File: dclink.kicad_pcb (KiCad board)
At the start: 2 copper layers, 61.5 x 59.5 mm, 3 parts, among them U1 mounting_holes, U2 dcb-310

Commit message: better shape
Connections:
- net Net-(U1-Pad) renamed GND
- U1 pad 2: Net-(U1-Pad)_1 -> VDC
- U2 pad 3: Net-(U1-Pad)_1 -> VDC
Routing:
- net VDC: vias 0 -> 60
- net Net-(U1-Pad)_1: vias 60 -> 0
- added copper zone on B.Cu, net VDC
- added copper zone on F.Cu, net VDC
- removed copper zone on B.Cu, net Net-(U1-Pad)_1
- removed copper zone on F.Cu, net Net-(U1-Pad)_1
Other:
- outline, holes or cut-outs redrawn

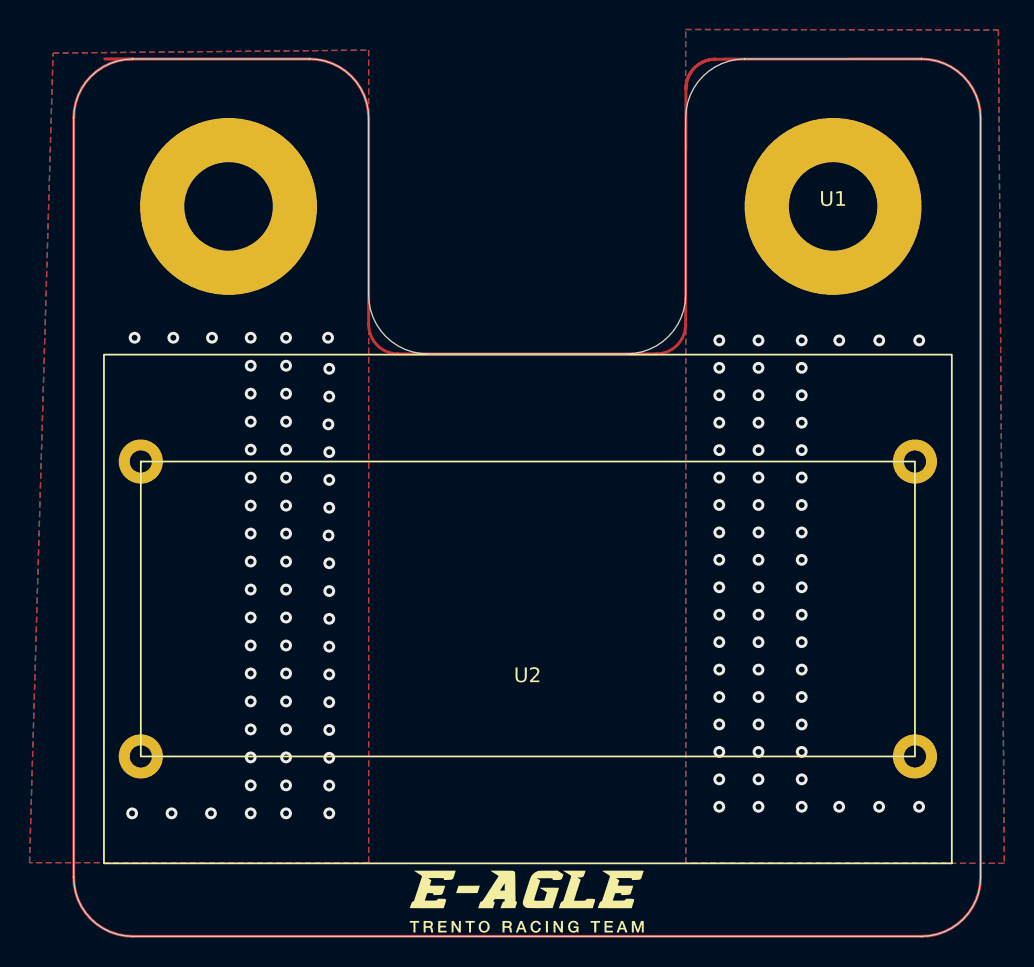
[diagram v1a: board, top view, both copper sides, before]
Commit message: first half vias, todo: top border
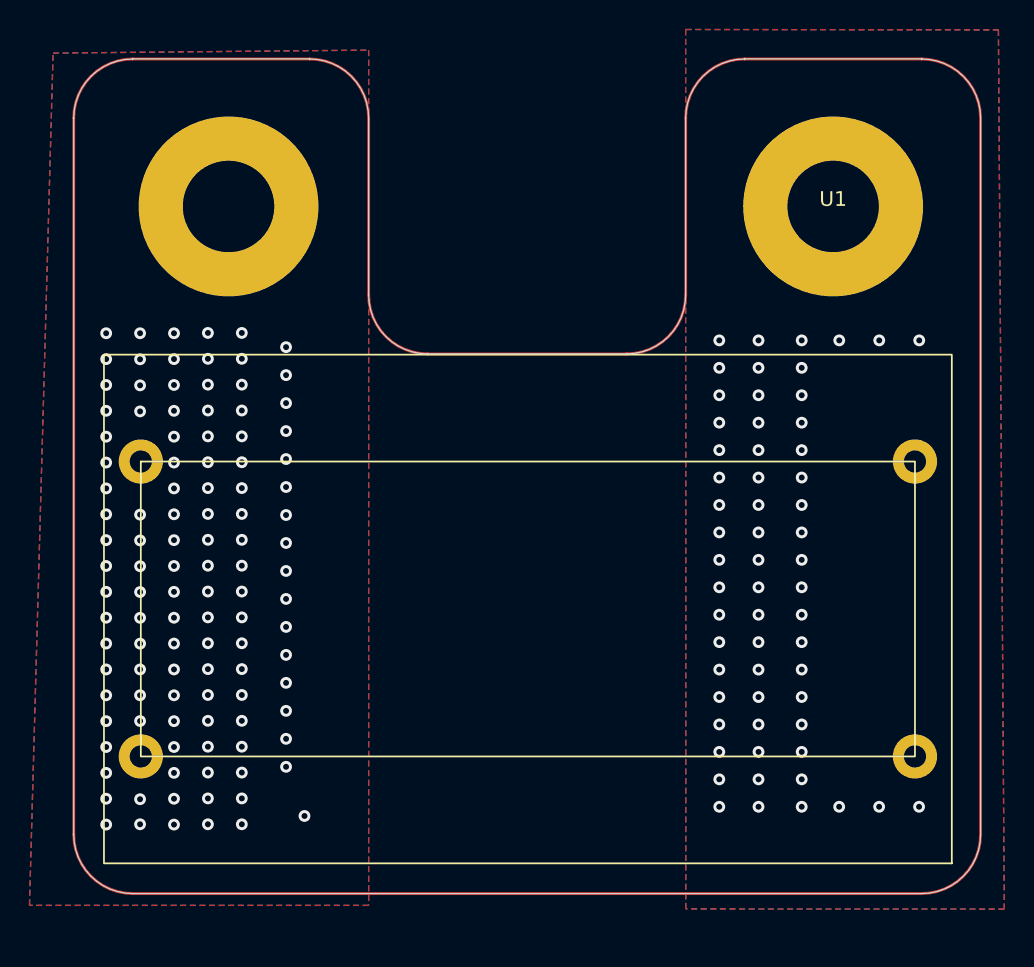
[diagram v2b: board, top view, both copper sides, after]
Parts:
- removed the   at (149.9, 131.6)
-  : renamed from U2
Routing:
- net GND: vias 60 -> 112
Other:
- board size 61.5 x 59.5 mm -> 61.5 x 56.6 mm

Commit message: done top border, first attempt vias
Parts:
- moved U1 1.00 mm to (170.6, 85.5)
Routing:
- net VDC: vias 60 -> 75
- net GND: vias 112 -> 75
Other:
- board size 61.5 x 56.6 mm -> 61.5 x 54.6 mm
- board text added: "2.7mm is the distance between the mounting hole pad and the top border. The same distance is between the mounting hole pad and the capacitor"

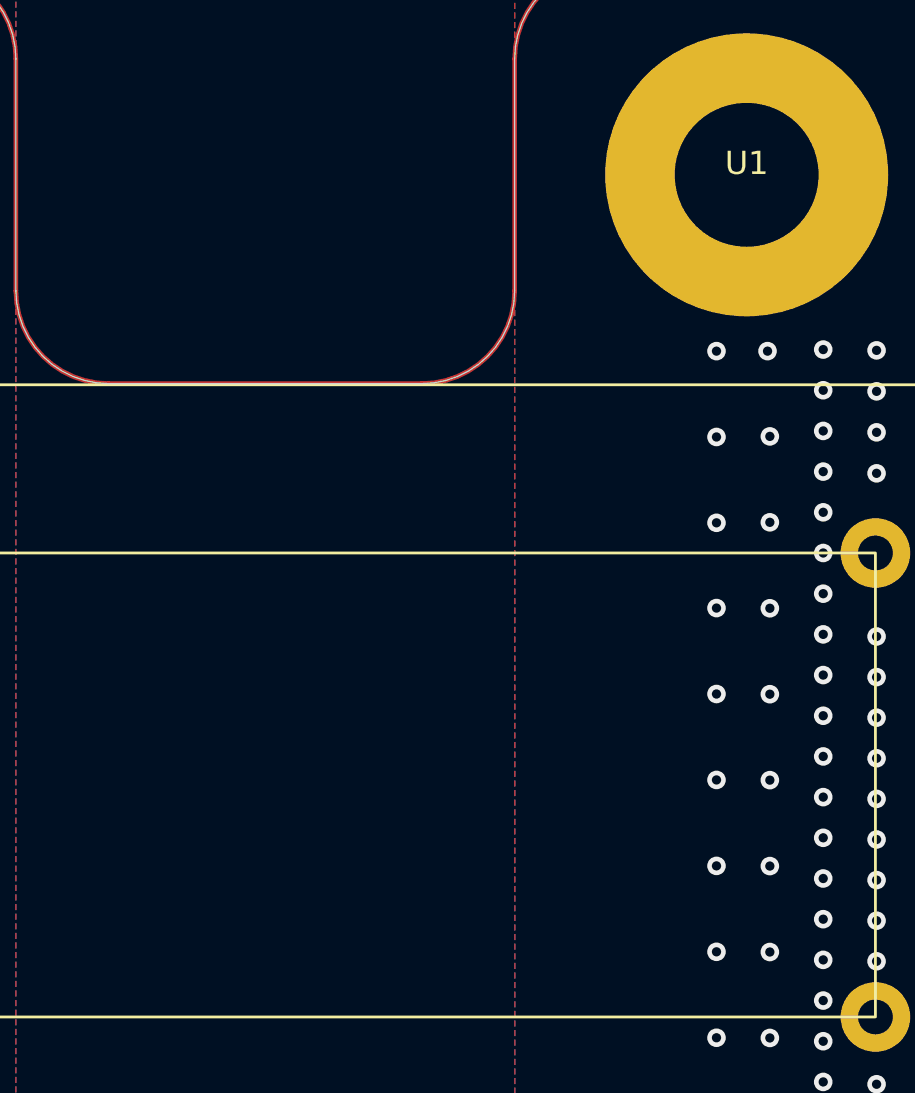
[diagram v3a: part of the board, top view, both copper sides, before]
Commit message: add logos
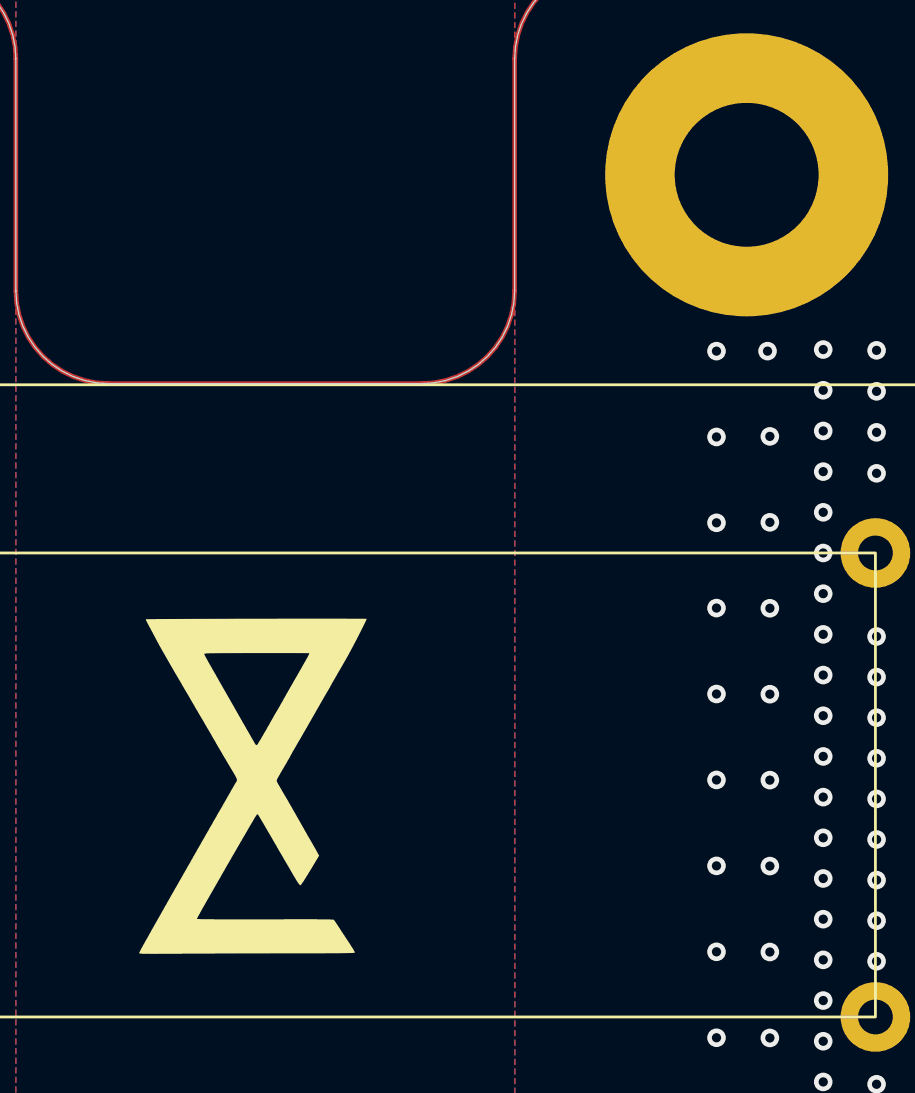
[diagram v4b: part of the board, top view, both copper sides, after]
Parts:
- added  : LOGO, LM393:logoleo, F.Cu at (149.3, 111.9)
- added  : LOGO, LM393:logototale, B.Cu at (149.3, 112.6)
-  : renamed from U1

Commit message: done logo, todo: check vias
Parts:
-  slow down: renamed from  
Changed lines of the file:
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@@
     (at 149.3 111.9)
     (attr board_only exclude_from_pos_files exclude_from_bom)
-    (fp_text reference " " (at -0.1 -20.7) (layer "F.SilkS")
+    (fp_text reference " slow down" (at -0.1 -13.7) (layer "F.SilkS")
       (effects (font (size 1.524 1.524) (thickness 0.3)))
     )
@@
   (gr_line (start 176.6 76.5) (end 164.6 76.5) (layer "Edge.Cuts") (width 0.05))
   (gr_arc (start 135.1 76.5) (mid 137.928427 77.671573) (end 139.1 80.5) (layer "Edge.Cuts") (width 0.05))
-  (gr_text "2.7mm is the distance between the mounting hole pad\nand the top border. The same distance is between the\nmounting hole pad and the capacitor\n" (at 173.5 72.1) (layer "Dwgs.User")
+  (gr_text "2.7mm is the distance between the mounting hole pad\nand the top border. The same distance is between the\nmounting hole pad and the capacitor\n" (at 148 70) (layer "Dwgs.User")
     (effects (font (size 1 1) (thickness 0.2)))
   )
@@
     (polygon
       (pts
-        (xy 181.81 72.53)
+        (xy 181.807022 74.635371)
         (xy 182.208566 132.150926)
         (xy 160.608566 132.140926)
-        (xy 160.6 72.5)
+        (xy 160.597022 74.605371)
       )
     )

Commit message: done logos
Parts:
- Hello there!: renamed from  slow down; value LOGO -> General Kenobi!
- moved   1.20 mm to (150.1, 111.7)
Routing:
- net VDC: vias 75 -> 85
- net GND: vias 75 -> 85

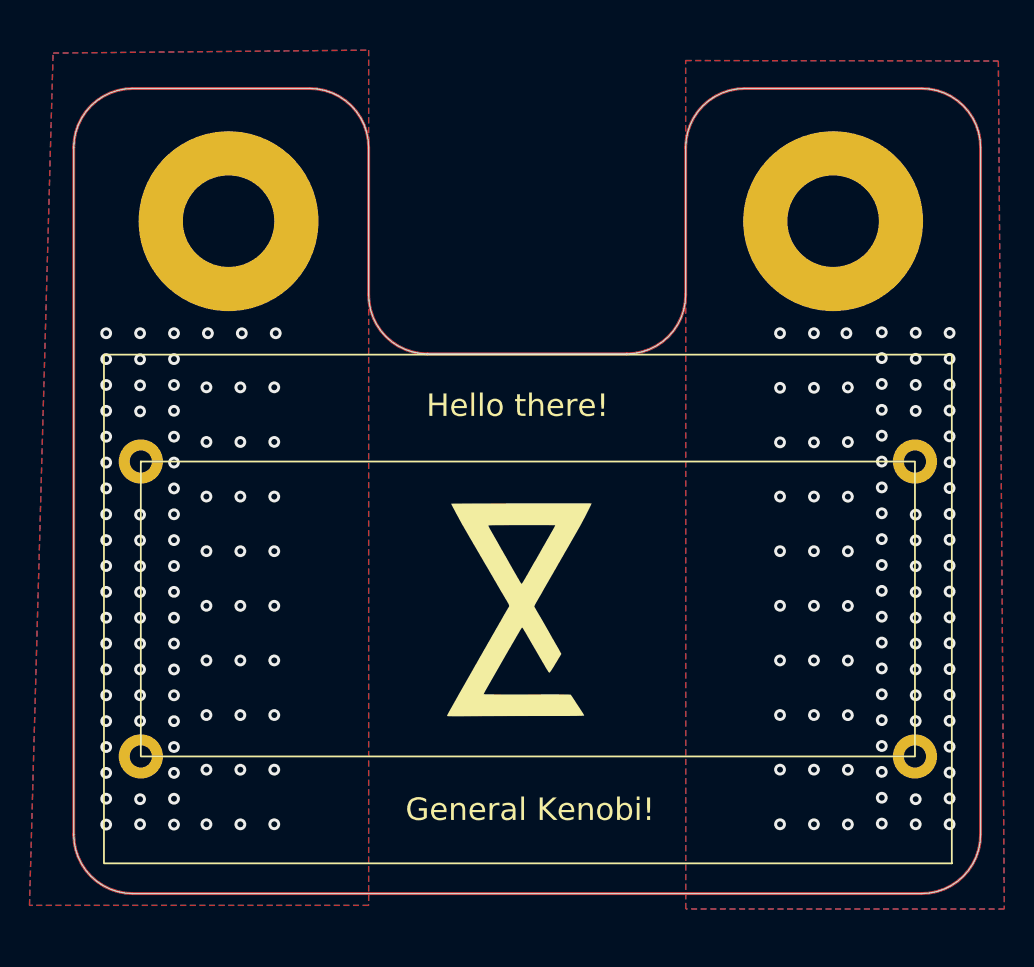
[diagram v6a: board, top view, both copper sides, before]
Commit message: done logos and top border
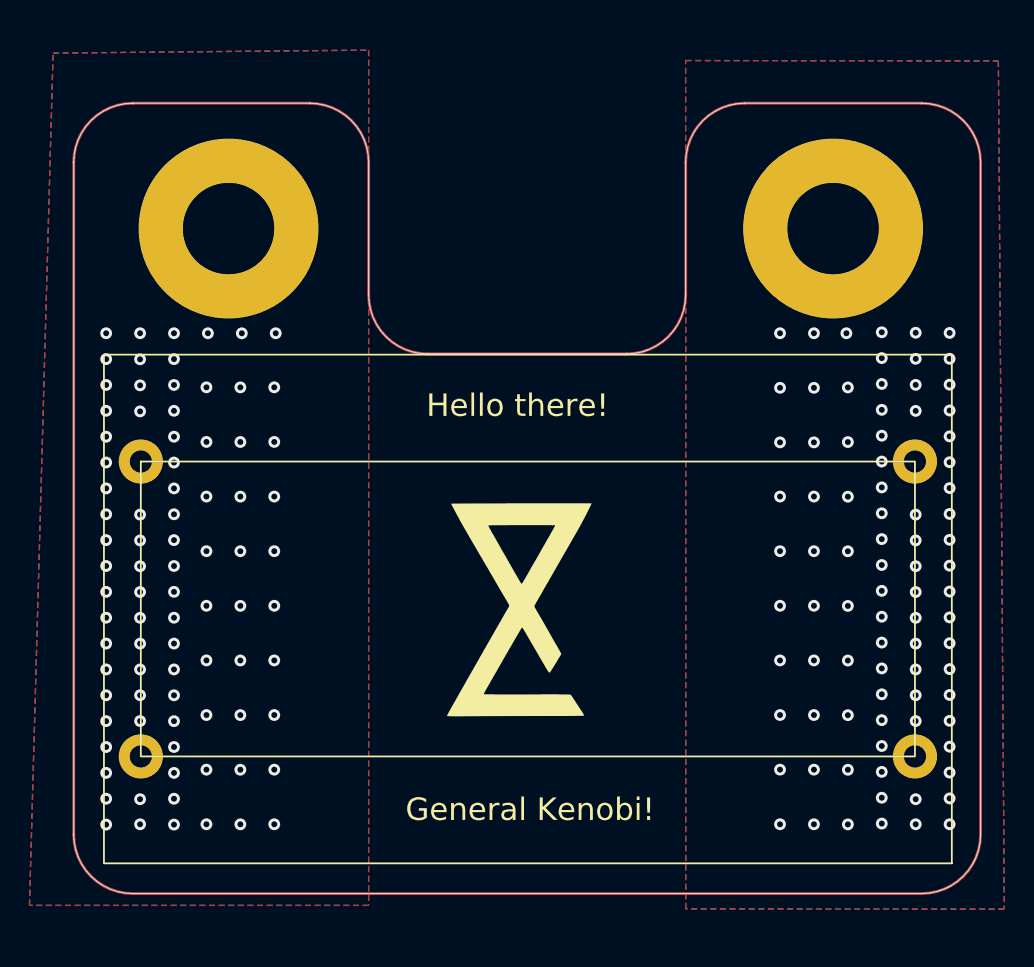
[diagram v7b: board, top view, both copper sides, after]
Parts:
- moved   0.50 mm to (170.6, 86.0)
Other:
- board size 61.5 x 54.6 mm -> 61.5 x 53.6 mm
- board text added: "CHECK:position of mounting holes: 86 or 86.5 in y: if the position of y is 86 there is the same distance between mounting hole and top bar and mounting hole and capacitor"
- board text removed: "2.7mm is the distance between the mounting hole pad and the top border. The same distance is between the mounting hole pad and the capacitor"
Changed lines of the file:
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@@
   (net 2 "VDC")
   (footprint "dcbk310:mounting_holes" (layer "F.Cu")
-    (at 170.6 85.5)
+    (at 170.6 86)
     (property "Sheetfile" "dclink.kicad_sch")
     (property "Sheetname" "")
@@
       ) (layer "B.SilkS") (width 0) (fill solid))
   )
-  (gr_line (start 176.6 76.5) (end 164.6 76.5) (layer "F.Cu") (width 0.2))
-  (gr_line (start 123.1 76.5) (end 135.1 76.5) (layer "F.Cu") (width 0.2))
-  (gr_arc (start 176.6 76.5) (mid 179.428427 77.671573) (end 180.6 80.5) (layer "F.Cu") (width 0.2))
+  (gr_line (start 176.6 77.5) (end 164.6 77.5) (layer "F.Cu") (width 0.2))
+  (gr_line (start 123.1 77.5) (end 135.1 77.5) (layer "F.Cu") (width 0.2))
+  (gr_arc (start 176.6 77.5) (mid 179.428427 78.671573) (end 180.6 81.5) (layer "F.Cu") (width 0.2))
   (gr_arc (start 143.1 94.5) (mid 140.271573 93.328427) (end 139.1 90.5) (layer "F.Cu") (width 0.2))
-  (gr_line (start 160.6 80.5) (end 160.6 90.5) (layer "F.Cu") (width 0.2))
+  (gr_line (start 160.6 81.5) (end 160.6 90.5) (layer "F.Cu") (width 0.2))
   (gr_arc (start 160.6 90.5) (mid 159.428427 93.328427) (end 156.6 94.5) (layer "F.Cu") (width 0.2))
-  (gr_line (start 119.1 80.5) (end 119.1 127.1) (layer "F.Cu") (width 0.2))
-  (gr_line (start 180.6 94.2) (end 180.6 80.5) (layer "F.Cu") (width 0.2))
+  (gr_line (start 119.1 81.5) (end 119.1 127.1) (layer "F.Cu") (width 0.2))
+  (gr_line (start 180.6 94.2) (end 180.6 81.5) (layer "F.Cu") (width 0.2))
   (gr_arc (start 123.1 131.1) (mid 120.271573 129.928427) (end 119.1 127.1) (layer "F.Cu") (width 0.2))
-  (gr_arc (start 135.1 76.5) (mid 137.928427 77.671573) (end 139.1 80.5) (layer "F.Cu") (width 0.2))
-  (gr_arc (start 119.1 80.5) (mid 120.271573 77.671573) (end 123.1 76.5) (layer "F.Cu") (width 0.2))
+  (gr_arc (start 135.1 77.5) (mid 137.928427 78.671573) (end 139.1 81.5) (layer "F.Cu") (width 0.2))
+  (gr_arc (start 119.1 81.5) (mid 120.271573 78.671573) (end 123.1 77.5) (layer "F.Cu") (width 0.2))
   (gr_line (start 180.6 127.1) (end 180.6 94.2) (layer "F.Cu") (width 0.2))
-  (gr_arc (start 160.6 80.5) (mid 161.771573 77.671573) (end 164.6 76.5) (layer "F.Cu") (width 0.2))
+  (gr_arc (start 160.6 81.5) (mid 161.771573 78.671573) (end 164.6 77.5) (layer "F.Cu") (width 0.2))
   (gr_arc (start 180.6 127.1) (mid 179.428427 129.928427) (end 176.6 131.1) (layer "F.Cu") (width 0.2))
-  (gr_line (start 139.1 80.5) (end 139.1 90.5) (layer "F.Cu") (width 0.2))
+  (gr_line (start 139.1 81.5) (end 139.1 90.5) (layer "F.Cu") (width 0.2))
   (gr_line (start 156.6 94.5) (end 143.1 94.5) (layer "F.Cu") (width 0.2))
   (gr_line (start 123.1 131.1) (end 176.6 131.1) (layer "F.Cu") (width 0.2))
-  (gr_line (start 135.1 76.5) (end 123.1 76.5) (layer "Edge.Cuts") (width 0.05))
+  (gr_line (start 135.1 77.5) (end 123.1 77.5) (layer "Edge.Cuts") (width 0.05))
   (gr_line (start 123.1 131.1) (end 176.6 131.1) (layer "Edge.Cuts") (width 0.05))
-  (gr_line (start 160.6 80.5) (end 160.6 90.5) (layer "Edge.Cuts") (width 0.05))
-  (gr_line (start 139.1 90.5) (end 139.1 80.5) (layer "Edge.Cuts") (width 0.05))
-  (gr_arc (start 160.6 80.5) (mid 161.771573 77.671573) (end 164.6 76.5) (layer "Edge.Cuts") (width 0.05))
+  (gr_line (start 160.6 81.5) (end 160.6 90.5) (layer "Edge.Cuts") (width 0.05))
+  (gr_line (start 139.1 90.5) (end 139.1 81.5) (layer "Edge.Cuts") (width 0.05))
+  (gr_arc (start 160.6 81.5) (mid 161.771573 78.671573) (end 164.6 77.5) (layer "Edge.Cuts") (width 0.05))
   (gr_line (start 156.6 94.5) (end 143.1 94.5) (layer "Edge.Cuts") (width 0.05))
-  (gr_arc (start 176.6 76.5) (mid 179.428427 77.671573) (end 180.6 80.5) (layer "Edge.Cuts") (width 0.05))
+  (gr_arc (start 176.6 77.5) (mid 179.428427 78.671573) (end 180.6 81.5) (layer "Edge.Cuts") (width 0.05))
   (gr_arc (start 160.6 90.5) (mid 159.428427 93.328427) (end 156.6 94.5) (layer "Edge.Cuts") (width 0.05))
   (gr_arc (start 180.6 127.1) (mid 179.428427 129.928427) (end 176.6 131.1) (layer "Edge.Cuts") (width 0.05))
-  (gr_arc (start 119.1 80.5) (mid 120.271573 77.671573) (end 123.1 76.5) (layer "Edge.Cuts") (width 0.05))
+  (gr_arc (start 119.1 81.5) (mid 120.271573 78.671573) (end 123.1 77.5) (layer "Edge.Cuts") (width 0.05))
   (gr_arc (start 143.1 94.5) (mid 140.271573 93.328427) (end 139.1 90.5) (layer "Edge.Cuts") (width 0.05))
-  (gr_line (start 180.6 127.1) (end 180.6 80.5) (layer "Edge.Cuts") (width 0.05))
-  (gr_line (start 119.1 80.5) (end 119.1 127.1) (layer "Edge.Cuts") (width 0.05))
+  (gr_line (start 180.6 127.1) (end 180.6 81.5) (layer "Edge.Cuts") (width 0.05))
+  (gr_line (start 119.1 81.5) (end 119.1 127.1) (layer "Edge.Cuts") (width 0.05))
   (gr_arc (start 123.1 131.1) (mid 120.271573 129.928427) (end 119.1 127.1) (layer "Edge.Cuts") (width 0.05))
-  (gr_line (start 176.6 76.5) (end 164.6 76.5) (layer "Edge.Cuts") (width 0.05))
-  (gr_arc (start 135.1 76.5) (mid 137.928427 77.671573) (end 139.1 80.5) (layer "Edge.Cuts") (width 0.05))
-  (gr_text "2.7mm is the distance between the mounting hole pad\nand the top border. The same distance is between the\nmounting hole pad and the capacitor\n" (at 148 70) (layer "Dwgs.User")
-    (effects (font (size 1 1) (thickness 0.2)))
+  (gr_line (start 176.6 77.5) (end 164.6 77.5) (layer "Edge.Cuts") (width 0.05))
+  (gr_arc (start 135.1 77.5) (mid 137.928427 78.671573) (end 139.1 81.5) (layer "Edge.Cuts") (width 0.05))
+  (gr_text "CHECK:position of mounting holes: 86 or 86.5 in y:\nif the position of y is 86 there is the same distance \nbetween mounting hole and top bar and mounting hole\nand capacitor " (at 150.3 66.6) (layer "Dwgs.User")
+    (effects (font (size 1.5 1.5) (thickness 0.3)))
   )
   (via (at 123.6 108.9) (size 0.8) (drill 0.4) (layers "F.Cu" "B.Cu") (free) (net 1))
